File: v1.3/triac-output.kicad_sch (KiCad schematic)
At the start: 7 parts, among them Q3 T835-600B, Q4 2N7002, U6 TLP160G

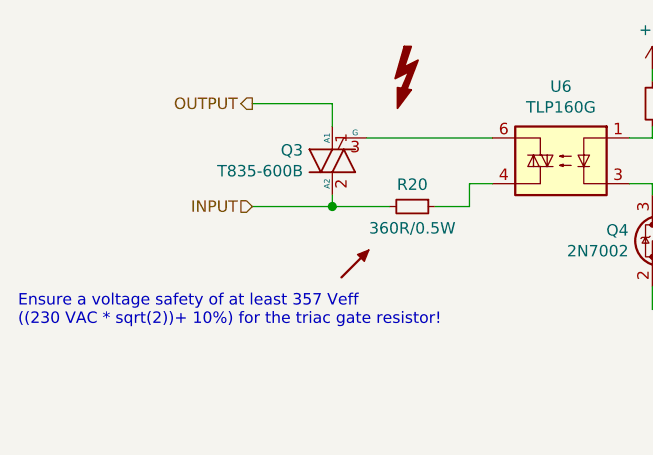
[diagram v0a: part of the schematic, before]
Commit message: Change TRIAC type in schematics
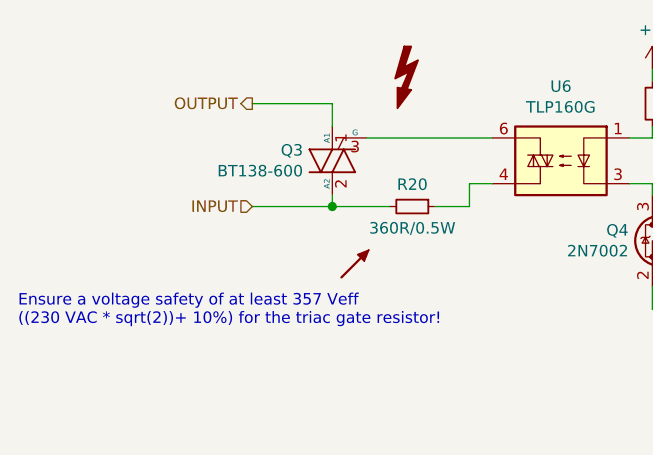
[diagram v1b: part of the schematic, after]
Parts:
- Q3: value T835-600B -> BT138-600
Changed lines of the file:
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@@
       (effects (font (size 1.27 1.27)) (justify left))
     )
-    (property "Value" "T835-600B" (id 1) (at 85.6488 53.213 0)
+    (property "Value" "BT138-600" (id 1) (at 85.6488 53.213 0)
       (effects (font (size 1.27 1.27)) (justify left))
     )
